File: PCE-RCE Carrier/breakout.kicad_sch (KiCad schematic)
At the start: 2 parts, among them J10 Conn_01x06_Pin, J6 PRT-16766

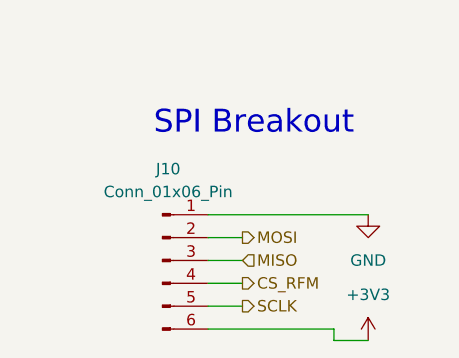
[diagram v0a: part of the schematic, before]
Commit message: added pinouts for board interface, b3b xh servo connector and 6v buck to ace carrier
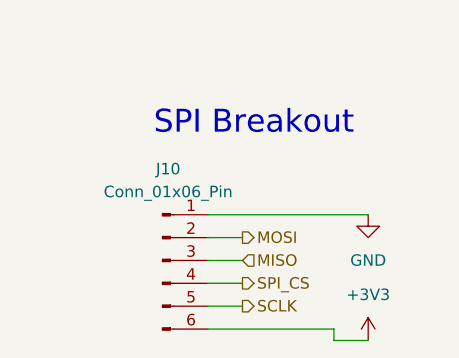
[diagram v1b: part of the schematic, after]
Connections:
- net CS_RFM renamed SPI_CS
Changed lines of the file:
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@@
 		)
 	)
-	(hierarchical_label "CS_RFM"
+	(hierarchical_label "SPI_CS"
 		(shape output)
 		(at 116.84 109.22 0)

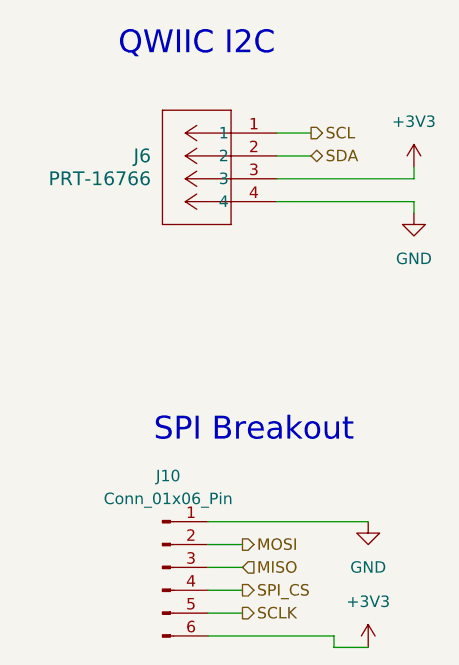
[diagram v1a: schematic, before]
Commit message: H-Bridge wiring + motor ports, cleaned up carrier schematics, added MISO source terminating resistors on carriers
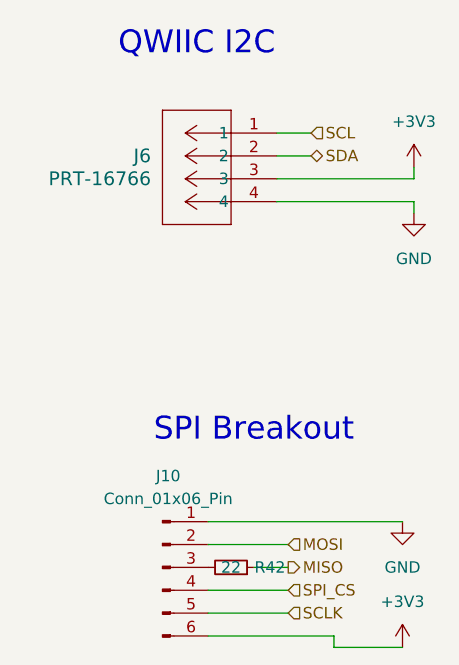
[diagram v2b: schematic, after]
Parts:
- added R42: 22, Resistor_SMD:R_0402_1005Metric, symbol Device:R_Small
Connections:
- net MISO: now also R42.1; no longer J10.3 (Pin_3)
- new net: J10.3 (Pin_3), R42.2
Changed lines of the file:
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@@
 	(wire
 		(pts
-			(xy 113.03 101.6) (xy 130.81 101.6)
+			(xy 113.03 101.6) (xy 134.62 101.6)
+		)
+		(stroke
+			(width 0)
+			(type default)
+		)
+	)
+	(wire
+		(pts
+			(xy 118.11 106.68) (xy 121.92 106.68)
 		)
 		(stroke
@@
 	(wire
 		(pts
-			(xy 116.84 111.76) (xy 113.03 111.76)
-		)
-		(stroke
-			(width 0)
-			(type default)
-		)
-	)
-	(wire
-		(pts
-			(xy 116.84 104.14) (xy 113.03 104.14)
-		)
-		(stroke
-			(width 0)
-			(type default)
-		)
-	)
-	(wire
-		(pts
-			(xy 116.84 106.68) (xy 113.03 106.68)
+			(xy 121.92 111.76) (xy 113.03 111.76)
+		)
+		(stroke
+			(width 0)
+			(type default)
+		)
+	)
+	(wire
+		(pts
+			(xy 121.92 104.14) (xy 113.03 104.14)
 		)
 		(stroke
@@
 	(wire
 		(pts
-			(xy 127 115.57) (xy 130.81 115.57)
+			(xy 127 115.57) (xy 134.62 115.57)
 		)
 		(stroke
@@
 	(wire
 		(pts
-			(xy 116.84 109.22) (xy 113.03 109.22)
+			(xy 121.92 109.22) (xy 113.03 109.22)
 		)
 		(stroke
@@
 	)
 	(hierarchical_label "SPI_CS"
-		(shape output)
-		(at 116.84 109.22 0)
+		(shape input)
+		(at 121.92 109.22 0)
 		(effects
 			(font
@@
 	)
 	(hierarchical_label "SCL"
-		(shape output)
+		(shape input)
 		(at 124.46 58.42 0)
 		(effects
@@
 	)
 	(hierarchical_label "MISO"
-		(shape input)
-		(at 116.84 106.68 0)
+		(shape output)
+		(at 121.92 106.68 0)
 		(effects
 			(font
@@
 	)
 	(hierarchical_label "SCLK"
-		(shape output)
-		(at 116.84 111.76 0)
+		(shape input)
+		(at 121.92 111.76 0)
 		(effects
 			(font
@@
 	)
 	(hierarchical_label "MOSI"
-		(shape output)
-		(at 116.84 104.14 0)
+		(shape input)
+		(at 121.92 104.14 0)
 		(effects
 			(font
@@
 	)
 	(symbol
+		(lib_id "Device:R_Small")
+		(at 115.57 106.68 270)
+		(mirror x)
+		(unit 1)
+		(body_style 1)
+		(exclude_from_sim no)
+		(in_bom yes)
+		(on_board yes)
+		(in_pos_files yes)
+		(dnp no)
+		(property "Reference" "R42"
+			(at 119.888 106.68 90)
+			(show_name no)
+			(do_not_autoplace no)
+			(effects
+				(font
+					(size 1.27 1.27)
+				)
+			)
+		)
+		(property "Value" "22"
+			(at 115.57 106.68 90)
+			(show_name no)
+			(do_not_autoplace no)
+			(effects
+				(font
+					(size 1.27 1.27)
+				)
+			)
+		)
+		(property "Footprint" "Resistor_SMD:R_0402_1005Metric"
+			(at 115.57 106.68 0)
+			(hide yes)
+			(show_name no)
+			(do_not_autoplace no)
+			(effects
+				(font
+					(size 1.27 1.27)
+				)
+			)
+		)
+		(property "Datasheet" ""
+			(at 115.57 106.68 0)
+			(hide yes)
+			(show_name no)
+			(do_not_autoplace no)
+			(effects
+				(font
+					(size 1.27 1.27)
+				)
+			)
+		)
+		(property "Description" "Resistor, small symbol"
+			(at 115.57 106.68 0)
+			(hide yes)
+			(show_name no)
+			(do_not_autoplace no)
+			(effects
+				(font
+					(size 1.27 1.27)
+				)
+			)
+		)
+		(pin "2"
+		)
+		(pin "1"
+		)
+		(instances
+			(project "PCE-RCE Carrier"
+				(path "/061bd5f9-7321-49d7-bd52-d55a9dc51a00/daaafe79-7dd1-4848-b9a2-db9d0b779713"
+					(reference "R42")
+					(unit 1)
+				)
+			)
+		)
+	)
+	(symbol
 		(lib_id "power:+3V3")
-		(at 130.81 115.57 0)
+		(at 134.62 115.57 0)
 		(unit 1)
 		(body_style 1)
@@
 		(fields_autoplaced yes)
 		(property "Reference" "#PWR072"
-			(at 130.81 119.38 0)
+			(at 134.62 119.38 0)
 			(hide yes)
 			(show_name no)
@@
 		)
 		(property "Value" "+3V3"
-			(at 130.81 110.49 0)
+			(at 134.62 110.49 0)
 			(show_name no)
 			(do_not_autoplace no)
@@
 		)
 		(property "Footprint" ""
-			(at 130.81 115.57 0)
+			(at 134.62 115.57 0)
 			(hide yes)
 			(show_name no)
@@
 		)
 		(property "Datasheet" ""
-			(at 130.81 115.57 0)
+			(at 134.62 115.57 0)
 			(hide yes)
 			(show_name no)
@@
 		)
 		(property "Description" "Power symbol creates a global label with name \"+3V3\""
-			(at 130.81 115.57 0)
+			(at 134.62 115.57 0)
 			(hide yes)
 			(show_name no)
@@
 	(symbol
 		(lib_id "power:GND")
-		(at 130.81 101.6 0)
+		(at 134.62 101.6 0)
 		(unit 1)
 		(body_style 1)
@@
 		(fields_autoplaced yes)
 		(property "Reference" "#PWR073"
-			(at 130.81 107.95 0)
+			(at 134.62 107.95 0)
 			(hide yes)
 			(show_name no)
@@
 		)
 		(property "Value" "GND"
-			(at 130.81 106.68 0)
+			(at 134.62 106.68 0)
 			(show_name no)
 			(do_not_autoplace no)
@@
 		)
 		(property "Footprint" ""
-			(at 130.81 101.6 0)
+			(at 134.62 101.6 0)
 			(hide yes)
 			(show_name no)
@@
 		)
 		(property "Datasheet" ""
-			(at 130.81 101.6 0)
+			(at 134.62 101.6 0)
 			(hide yes)
 			(show_name no)
@@
 		)
 		(property "Description" "Power symbol creates a global label with name \"GND\" , ground"
-			(at 130.81 101.6 0)
-			(hide yes)
-			(show_name no)
+			(at 134.62 101.6 0)
+			(hide yes)
+			(show_name no)

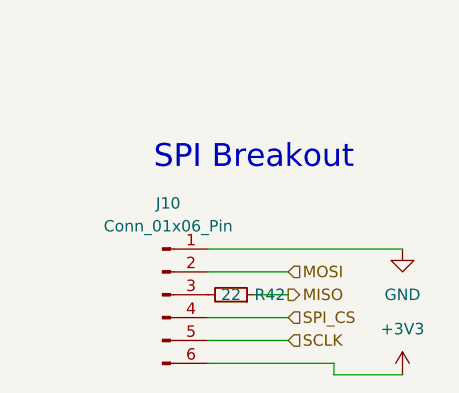
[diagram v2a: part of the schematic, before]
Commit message: mfw high power components are large
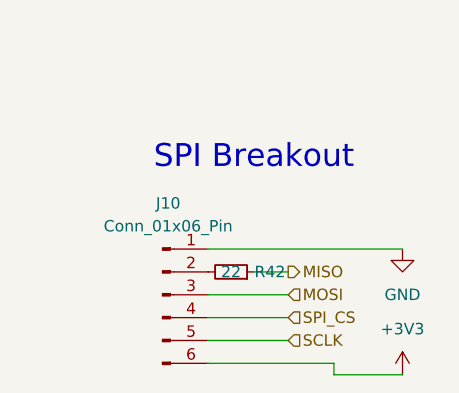
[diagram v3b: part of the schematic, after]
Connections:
- net MOSI: now also J10.3 (Pin_3); no longer J10.2 (Pin_2)
- net at R42.2: now also J10.2 (Pin_2); no longer J10.3 (Pin_3)
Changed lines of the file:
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@@
-	(wire
-		(pts
-			(xy 118.11 106.68) (xy 121.92 106.68)
-		)
-		(stroke
-			(width 0)
-			(type default)
-		)
-	)
 	(wire
 		(pts
@@
 	(wire
 		(pts
-			(xy 121.92 104.14) (xy 113.03 104.14)
-		)
-		(stroke
-			(width 0)
-			(type default)
-		)
-	)
-	(wire
-		(pts
 			(xy 135.89 66.04) (xy 135.89 67.31)
 		)
@@
 		(pts
 			(xy 127 115.57) (xy 127 114.3)
+		)
+		(stroke
+			(width 0)
+			(type default)
+		)
+	)
+	(wire
+		(pts
+			(xy 118.11 104.14) (xy 121.92 104.14)
+		)
+		(stroke
+			(width 0)
+			(type default)
+		)
+	)
+	(wire
+		(pts
+			(xy 121.92 106.68) (xy 113.03 106.68)
 		)
 		(stroke
@@
 		)
 	)
-	(hierarchical_label "MISO"
-		(shape output)
-		(at 121.92 106.68 0)
-		(effects
-			(font
-				(size 1.27 1.27)
-			)
-			(justify left)
-		)
-	)
 	(hierarchical_label "SCLK"
 		(shape input)
@@
 	(hierarchical_label "MOSI"
 		(shape input)
+		(at 121.92 106.68 0)
+		(effects
+			(font
+				(size 1.27 1.27)
+			)
+			(justify left)
+		)
+	)
+	(hierarchical_label "MISO"
+		(shape output)
 		(at 121.92 104.14 0)
 		(effects
@@
 	)
 	(symbol
-		(lib_id "Device:R_Small")
-		(at 115.57 106.68 270)
-		(mirror x)
-		(unit 1)
-		(body_style 1)
-		(exclude_from_sim no)
-		(in_bom yes)
-		(on_board yes)
-		(in_pos_files yes)
-		(dnp no)
-		(property "Reference" "R42"
-			(at 119.888 106.68 90)
-			(show_name no)
-			(do_not_autoplace no)
-			(effects
-				(font
-					(size 1.27 1.27)
-				)
-			)
-		)
-		(property "Value" "22"
-			(at 115.57 106.68 90)
-			(show_name no)
-			(do_not_autoplace no)
-			(effects
-				(font
-					(size 1.27 1.27)
-				)
-			)
-		)
-		(property "Footprint" "Resistor_SMD:R_0402_1005Metric"
-			(at 115.57 106.68 0)
-			(hide yes)
-			(show_name no)
-			(do_not_autoplace no)
-			(effects
-				(font
-					(size 1.27 1.27)
-				)
-			)
-		)
-		(property "Datasheet" ""
-			(at 115.57 106.68 0)
-			(hide yes)
-			(show_name no)
-			(do_not_autoplace no)
-			(effects
-				(font
-					(size 1.27 1.27)
-				)
-			)
-		)
-		(property "Description" "Resistor, small symbol"
-			(at 115.57 106.68 0)
-			(hide yes)
-			(show_name no)
-			(do_not_autoplace no)
-			(effects
-				(font
-					(size 1.27 1.27)
-				)
-			)
-		)
-		(pin "2"
-		)
-		(pin "1"
-		)
-		(instances
-			(project "PCE-RCE Carrier"
-				(path "/061bd5f9-7321-49d7-bd52-d55a9dc51a00/daaafe79-7dd1-4848-b9a2-db9d0b779713"
-					(reference "R42")
-					(unit 1)
-				)
-			)
-		)
-	)
-	(symbol
 		(lib_id "power:+3V3")
 		(at 134.62 115.57 0)
@@
 					(unit 1)
 				)
+			)
+		)
+	)
+	(symbol
+		(lib_id "Device:R_Small")
+		(at 115.57 104.14 270)
+		(mirror x)
+		(unit 1)
+		(body_style 1)
+		(exclude_from_sim no)
+		(in_bom yes)
+		(on_board yes)
+		(in_pos_files yes)
+		(dnp no)
+		(property "Reference" "R42"
+			(at 119.888 104.14 90)
+			(show_name no)
+			(do_not_autoplace no)
+			(effects
+				(font
+					(size 1.27 1.27)
+				)
+			)
+		)
+		(property "Value" "22"
+			(at 115.57 104.14 90)
+			(show_name no)
+			(do_not_autoplace no)
+			(effects
+				(font
+					(size 1.27 1.27)
+				)
+			)
+		)
+		(property "Footprint" "Resistor_SMD:R_0402_1005Metric"
+			(at 115.57 104.14 0)
+			(hide yes)
+			(show_name no)
+			(do_not_autoplace no)
+			(effects
+				(font
+					(size 1.27 1.27)
+				)
+			)
+		)
+		(property "Datasheet" ""
+			(at 115.57 104.14 0)
+			(hide yes)
+			(show_name no)
+			(do_not_autoplace no)
+			(effects
+				(font
+					(size 1.27 1.27)
+				)
+			)
+		)
+		(property "Description" "Resistor, small symbol"
+			(at 115.57 104.14 0)
+			(hide yes)
+			(show_name no)
+			(do_not_autoplace no)
+			(effects
+				(font
+					(size 1.27 1.27)
+				)
+			)
+		)
+		(pin "2"
+		)
+		(pin "1"
+		)
+		(instances
+			(project "PCE-RCE Carrier"
+				(path "/061bd5f9-7321-49d7-bd52-d55a9dc51a00/daaafe79-7dd1-4848-b9a2-db9d0b779713"
+					(reference "R42")
+					(unit 1)
+				)

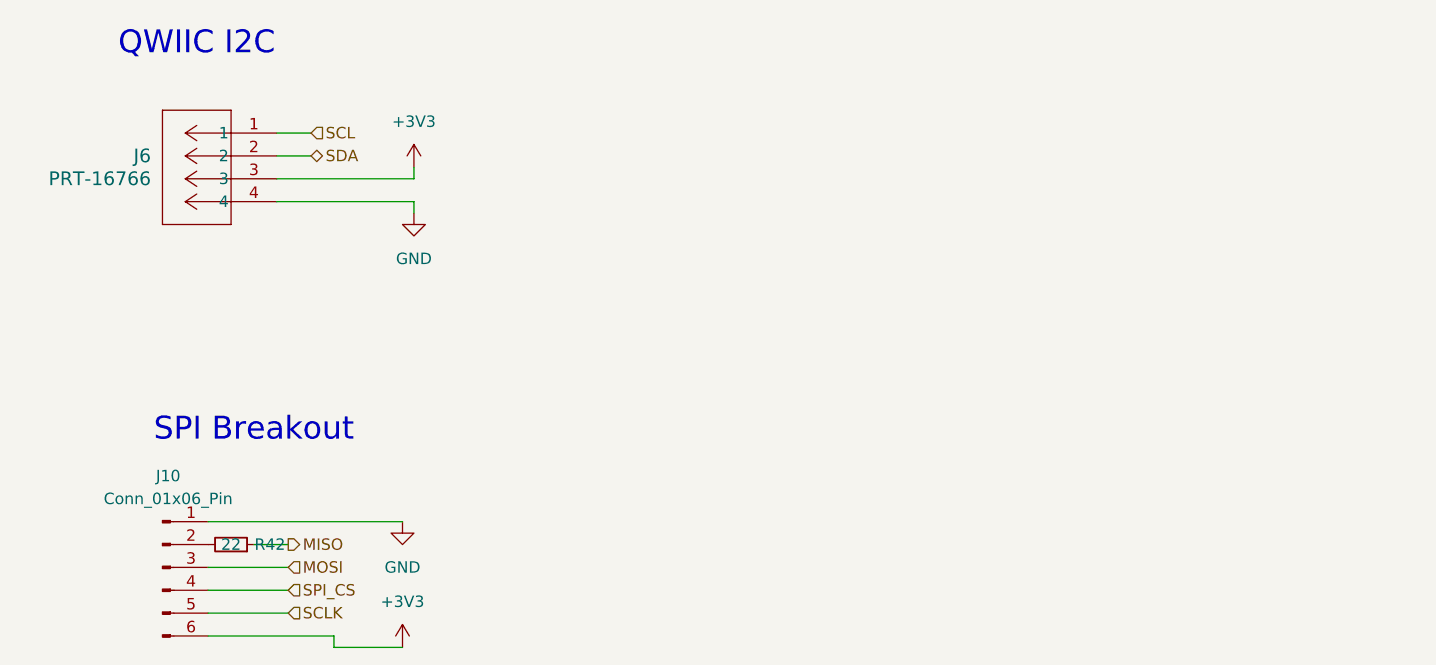
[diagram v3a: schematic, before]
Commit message: updated pyro circuit to be like easymini, lowk will prob make it a separate carrier
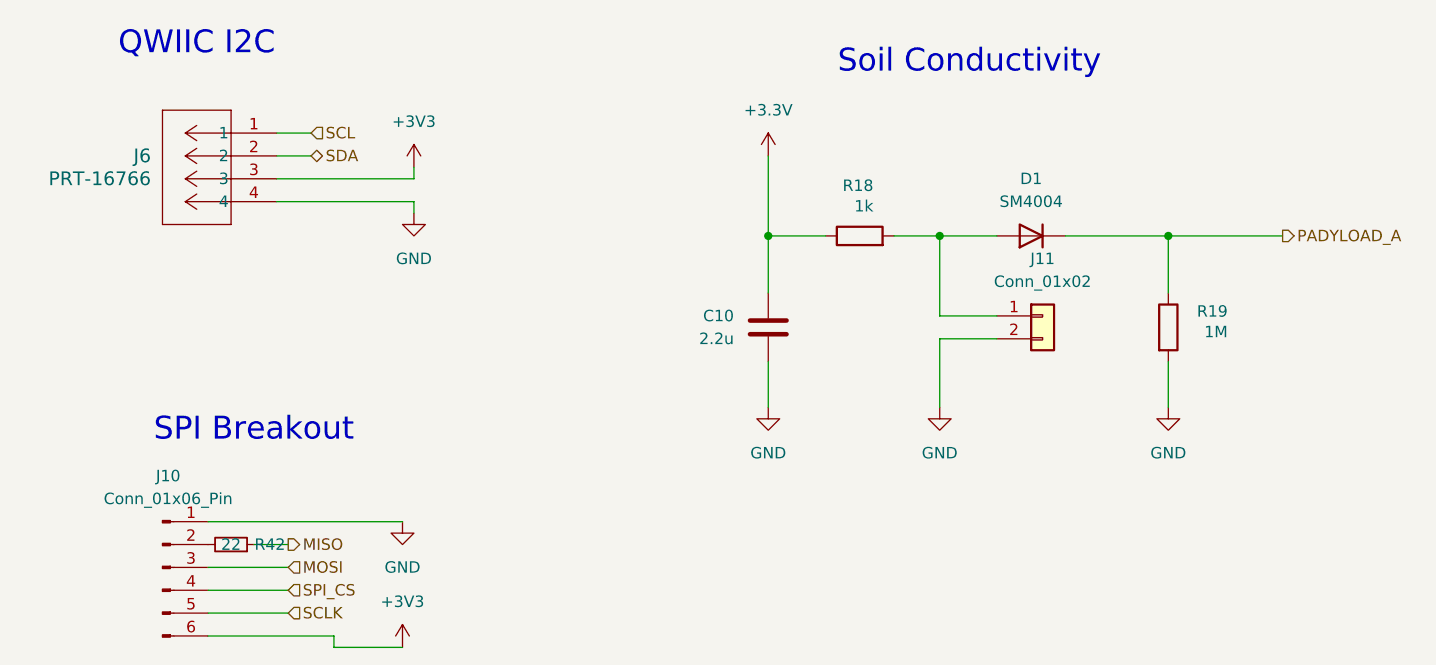
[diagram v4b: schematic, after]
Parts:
- added C10: 2.2u, Capacitor_SMD:C_0805_2012Metric, symbol Device:C
- added D1: SM4004, Diode_SMD:D_MELF, symbol Diode:SM4004
- added J11: Conn_01x02, Connector_PinSocket_2.54mm:PinSocket_1x02_P2.54mm_Vertical, symbol Connector_Generic:Conn_01x02
- added R18: 1k, Resistor_SMD:R_0402_1005Metric, symbol Device:R
- added R19: 1M, Resistor_SMD:R_0402_1005Metric, symbol Device:R
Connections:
- net GND: now also C10.2, J11.2 (Pin_2), R19.2
- new net: D1.2 (A), J11.1 (Pin_1), R18.2
- new net +3.3V: C10.1, R18.1
- new net PADYLOAD_A: D1.1 (K), R19.1
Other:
- note added: "Soil Conductivity"

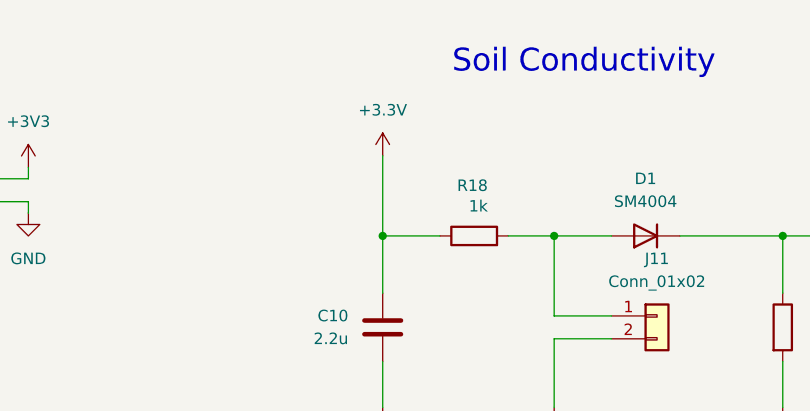
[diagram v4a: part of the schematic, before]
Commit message: split pce and rce functions into two carriers, initial rce parts placement
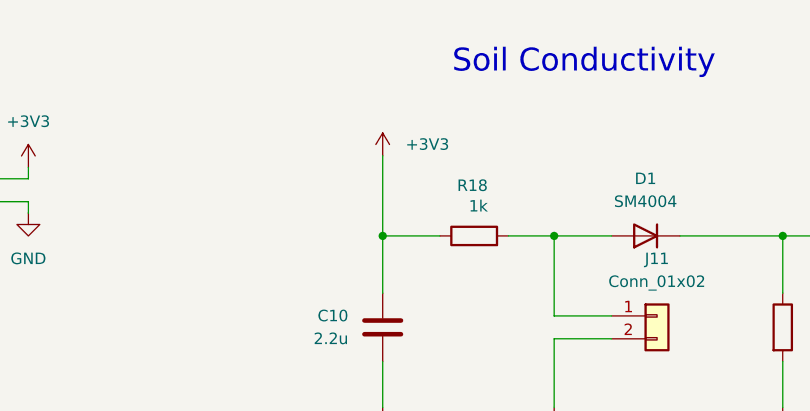
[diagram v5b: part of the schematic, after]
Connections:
- net +3.3V is gone; now on net +3V3: C10.1, R18.1
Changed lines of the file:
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@@
 			)
 		)
-		(property "Value" "+3.3V"
-			(at 175.26 55.88 0)
+		(property "Value" "+3V3"
+			(at 177.8 59.6899 0)
 			(show_name no)
 			(do_not_autoplace no)
@@
 					(size 1.27 1.27)
 				)
+				(justify left)
 			)
 		)

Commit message: DRC changes and updated fab files
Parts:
- J10: footprint Connector_PinSocket_2.54mm:PinSocket_1x06_P2.54mm_Vertical -> Connector_PinHeader_2.54mm:PinHeader_1x06_P2.54mm_Vertical
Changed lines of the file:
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@@
 			)
 		)
-		(property "Footprint" "Connector_PinSocket_2.54mm:PinSocket_1x06_P2.54mm_Vertical"
+		(property "Footprint" "Connector_PinHeader_2.54mm:PinHeader_1x06_P2.54mm_Vertical"
 			(at 107.95 106.68 0)
 			(hide yes)
